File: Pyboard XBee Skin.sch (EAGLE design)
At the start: 8 parts

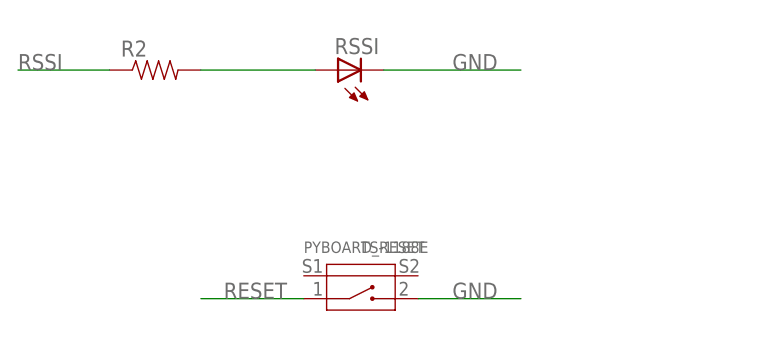
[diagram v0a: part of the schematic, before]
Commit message: Eagle CAD schematic file v1.2
new reset button
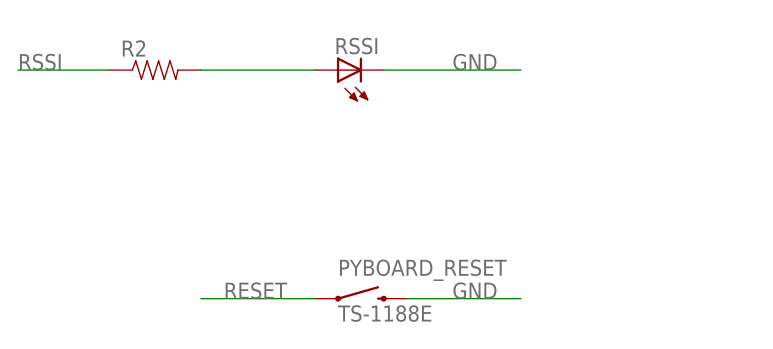
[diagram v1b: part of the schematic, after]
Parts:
- PYBOARD_RESET: device Seeed-OPL-Button:SMD-BUTTON-2+2P -> SparkFun-Electromechanical:SWITCH-MOMENTARY-2SMD
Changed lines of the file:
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@@
 <part name="R1" library="SparkFun-Passives" deviceset="RESISTOR" device="0603-RES"/>
 <part name="R2" library="SparkFun-Passives" deviceset="RESISTOR" device="0603-RES"/>
-<part name="PYBOARD_RESET" library="Seeed-OPL-Button" deviceset="SMD-BUTTON-2+2P" device="" value="TS-1188E"/>
+<part name="PYBOARD_RESET" library="SparkFun-Electromechanical" deviceset="SWITCH-MOMENTARY-2" device="SMD" value="TS-1188E"/>
 </parts>
 <sheets>
@@
 <instance part="R1" gate="G$1" x="58.42" y="66.04"/>
 <instance part="R2" gate="G$1" x="58.42" y="48.26"/>
-<instance part="PYBOARD_RESET" gate="K" x="81.28" y="24.13"/>
+<instance part="PYBOARD_RESET" gate="G$1" x="81.28" y="22.86"/>
 </instances>
 <busses>
@@
 </segment>
 <segment>
-<pinref part="PYBOARD_RESET" gate="K" pin="2"/>
-<wire x1="87.63" y1="22.86" x2="99.06" y2="22.86" width="0.1524" layer="91"/>
+<pinref part="PYBOARD_RESET" gate="G$1" pin="2"/>
+<wire x1="86.36" y1="22.86" x2="99.06" y2="22.86" width="0.1524" layer="91"/>
 <label x="91.44" y="22.86" size="1.778" layer="95"/>
 </segment>
@@
 </segment>
 <segment>
-<pinref part="PYBOARD_RESET" gate="K" pin="1"/>
-<wire x1="74.93" y1="22.86" x2="63.5" y2="22.86" width="0.1524" layer="91"/>
+<pinref part="PYBOARD_RESET" gate="G$1" pin="1"/>
+<wire x1="76.2" y1="22.86" x2="63.5" y2="22.86" width="0.1524" layer="91"/>
 <label x="66.04" y="22.86" size="1.778" layer="95"/>
 </segment>
